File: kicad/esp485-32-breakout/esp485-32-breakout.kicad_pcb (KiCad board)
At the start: 2 copper layers, 25.4 x 26.7 mm, 13 parts, among them J1 Conn_01x08, J2 Conn_01x08, U1 MAX3485, U2 ESP-WROOM-32, U3 AMS1117-3.3

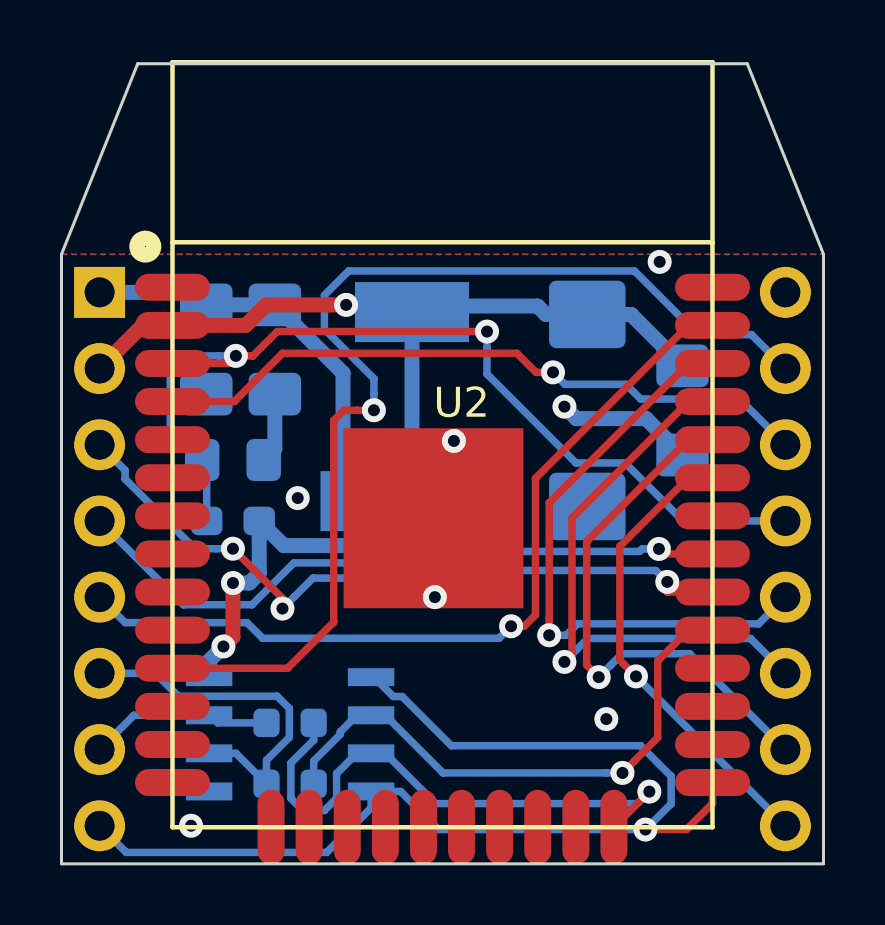
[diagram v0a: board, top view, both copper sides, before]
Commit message: Use hardware UART for RS485 in ESP32
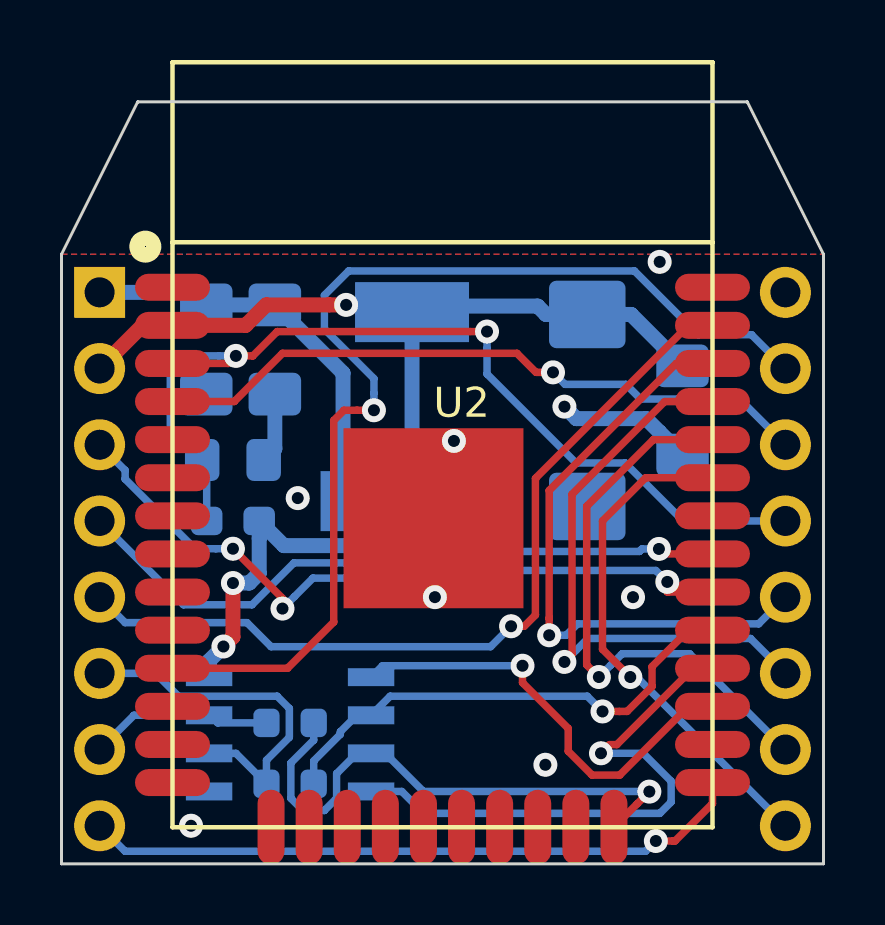
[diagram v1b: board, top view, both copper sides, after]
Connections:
- U1 pad 1: IO0 -> /IO16
- U1 pad 4: IO0 -> /IO17
- U2 pad 27: Net-(U2-Pad27) -> /IO16
- U2 pad 28: Net-(U2-Pad28) -> /IO17
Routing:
- net /IO17: track 0.00 -> 18.8 mm, vias 0 -> 1
- net IO0: track 37.0 -> 22.1 mm
- net /IO16: track 0.00 -> 14.8 mm, vias 0 -> 1
- net IO5: track 19.0 -> 16.7 mm
- net SDA: track 15.6 -> 17.1 mm
- net RXD: track 18.2 -> 18.8 mm
- net GND: vias 7 -> 8
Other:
- board size 25.4 x 26.7 mm -> 25.4 x 25.4 mm
